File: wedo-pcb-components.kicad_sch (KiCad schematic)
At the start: 1 part, among them U1 TPS61032

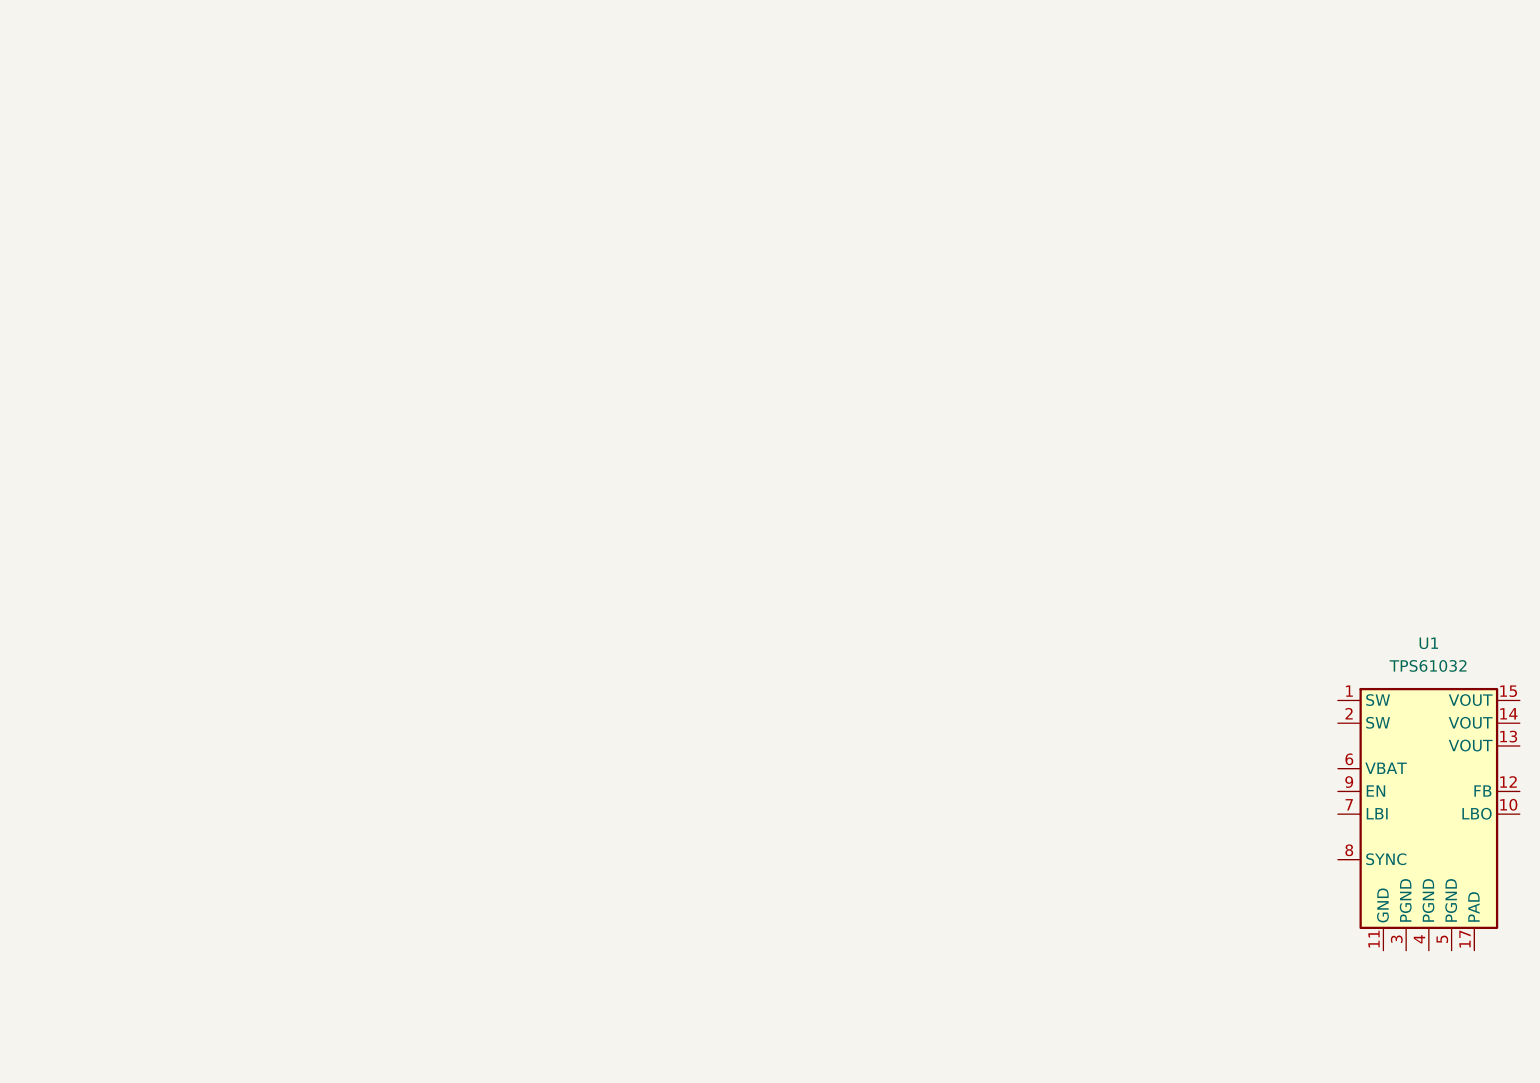
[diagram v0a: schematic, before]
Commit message: Add 6p6c connector footprint and adjust PCB geometry with mounting holes
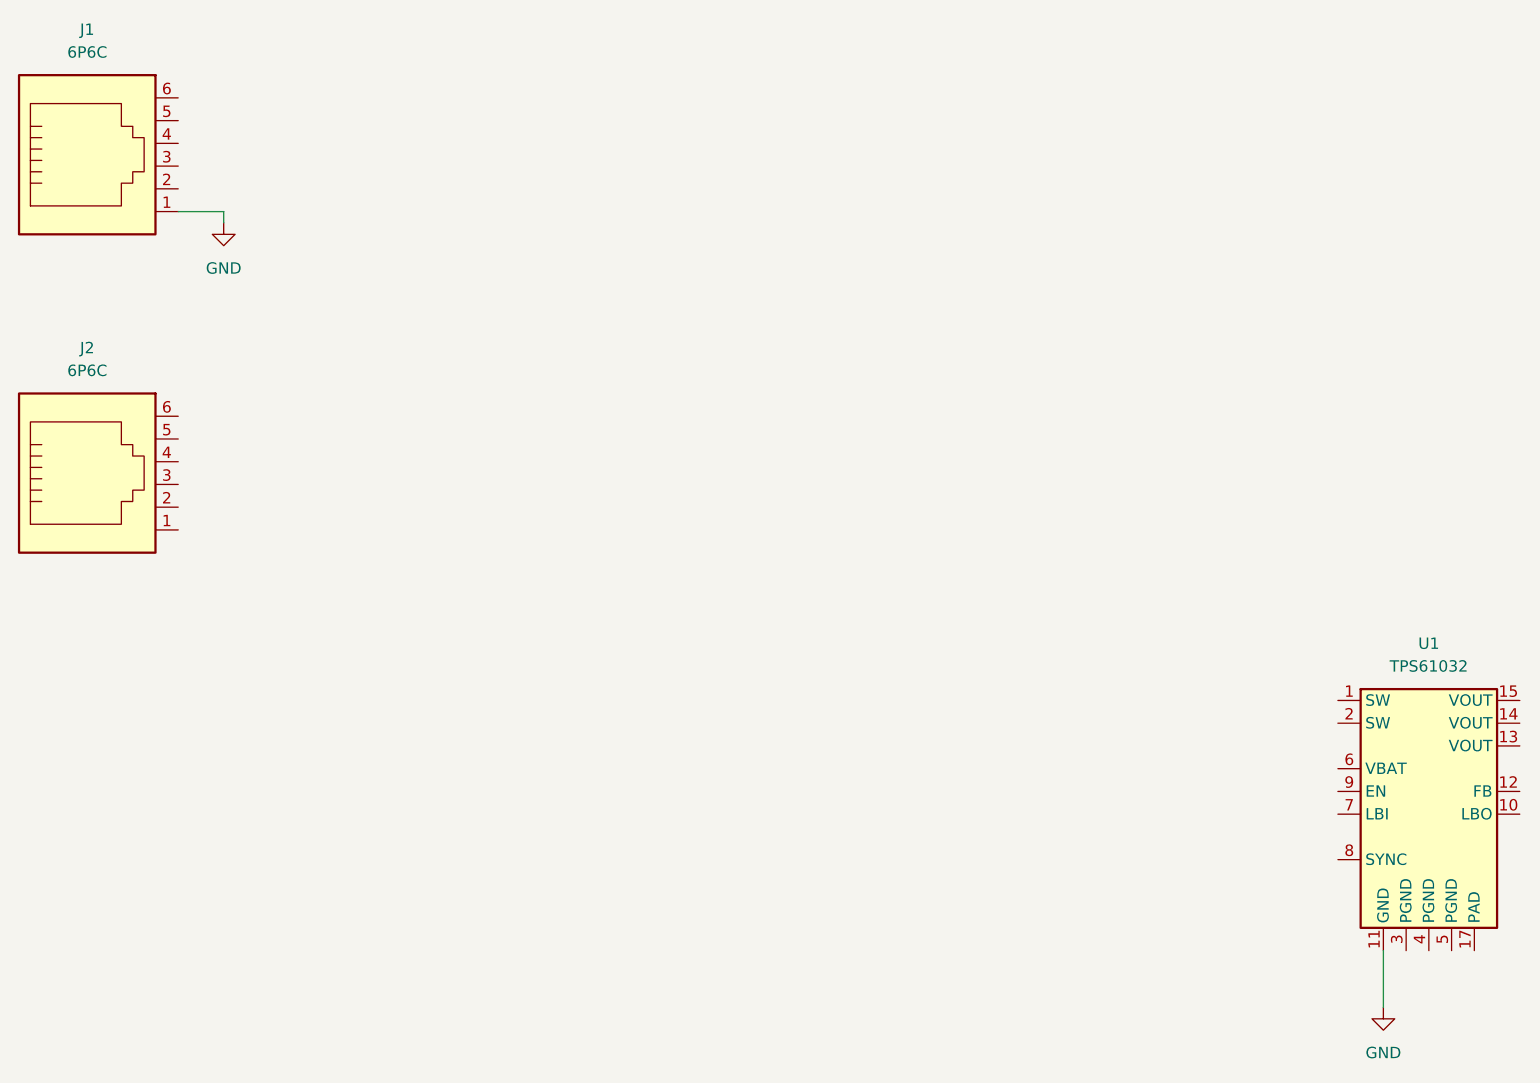
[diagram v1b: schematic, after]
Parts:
- added J1, J2: 6P6C, Connector_RJ_wedo:RJ12_wedo, symbol Connector:6P6C
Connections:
- net GND: now reaches U1.11 (GND)
- net GND: now also J1.1
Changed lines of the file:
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@@
 (kicad_sch (version 20230121) (generator eeschema)
   (paper "A4")
+  (wire (pts (xy 203.2 147.32) (xy 203.2 153.67))
+    (stroke (width 0) (type default))
+  )
+  (wire (pts (xy 73.66 64.77) (xy 73.66 66.04))
+    (stroke (width 0) (type default))
+  )
+  (wire (pts (xy 68.58 64.77) (xy 73.66 64.77))
+    (stroke (width 0) (type default))
+  )
   (symbol (lib_id "Regulator_Switching_Boost:TPS61032") (at 208.28 132.08 0) (unit 1)
     (in_bom yes) (on_board yes) (dnp no) (fields_autoplaced)
@@
         )
       )
+    )
+  )
+  (symbol (lib_id "power:GND") (at 203.2 153.67 0) (unit 1)
+    (in_bom yes) (on_board yes) (dnp no) (fields_autoplaced)
+    (property "Reference" "#PWR01" (at 203.2 160.02 0)
+      (effects (font (size 1.27 1.27)) hide)
+    )
+    (property "Value" "GND" (at 203.2 158.75 0)
+      (effects (font (size 1.27 1.27)))
+    )
+    (property "Footprint" "" (at 203.2 153.67 0)
+      (effects (font (size 1.27 1.27)) hide)
+    )
+    (property "Datasheet" "" (at 203.2 153.67 0)
+      (effects (font (size 1.27 1.27)) hide)
+    )
+    (pin "1")
+    (instances
+      (project "wedo-pcb-components"
+        (path "/3b24d53b-e226-431a-952a-6b8641a91fb3"
+          (reference "#PWR01") (unit 1)
+        )
+      )
+    )
+  )
+  (symbol (lib_id "power:GND") (at 73.66 66.04 0) (unit 1)
+    (in_bom yes) (on_board yes) (dnp no) (fields_autoplaced)
+    (property "Reference" "#PWR02" (at 73.66 72.39 0)
+      (effects (font (size 1.27 1.27)) hide)
+    )
+    (property "Value" "GND" (at 73.66 71.12 0)
+      (effects (font (size 1.27 1.27)))
+    )
+    (property "Footprint" "" (at 73.66 66.04 0)
+      (effects (font (size 1.27 1.27)) hide)
+    )
+    (property "Datasheet" "" (at 73.66 66.04 0)
+      (effects (font (size 1.27 1.27)) hide)
+    )
+    (pin "1")
+    (instances
+      (project "wedo-pcb-components"
+        (path "/3b24d53b-e226-431a-952a-6b8641a91fb3"
+          (reference "#PWR02") (unit 1)
+        )
+      )
+    )
+  )
+  (symbol (lib_id "Connector:6P6C") (at 58.42 95.25 0) (unit 1)
+    (in_bom yes) (on_board yes) (dnp no) (fields_autoplaced)
+    (property "Reference" "J2" (at 58.42 80.01 0)
+      (effects (font (size 1.27 1.27)))
+    )
+    (property "Value" "6P6C" (at 58.42 82.55 0)
+      (effects (font (size 1.27 1.27)))
+    )
+    (property "Footprint" "Connector_RJ_wedo:RJ12_wedo" (at 58.42 94.615 90)
+      (effects (font (size 1.27 1.27)) hide)
+    )
+    (property "Datasheet" "~" (at 58.42 94.615 90)
+      (effects (font (size 1.27 1.27)) hide)
+    )
+    (pin "3")
+    (pin "2")
+    (pin "4")
+    (pin "5")
+    (pin "6")
+    (pin "1")
+    (instances
+      (project "wedo-pcb-components"
+        (path "/3b24d53b-e226-431a-952a-6b8641a91fb3"
+          (reference "J2") (unit 1)
+        )
+      )
+    )
+  )
+  (symbol (lib_id "Connector:6P6C") (at 58.42 59.69 0) (unit 1)
+    (in_bom yes) (on_board yes) (dnp no) (fields_autoplaced)
+    (property "Reference" "J1" (at 58.42 44.45 0)
+      (effects (font (size 1.27 1.27)))
+    )
+    (property "Value" "6P6C" (at 58.42 46.99 0)
+      (effects (font (size 1.27 1.27)))
+    )
+    (property "Footprint" "Connector_RJ_wedo:RJ12_wedo" (at 58.42 59.055 90)
+      (effects (font (size 1.27 1.27)) hide)
+    )
+    (property "Datasheet" "~" (at 58.42 59.055 90)
+      (effects (font (size 1.27 1.27)) hide)
+    )
+    (pin "3")
+    (pin "2")
+    (pin "4")
+    (pin "5")
+    (pin "6")
+    (pin "1")
+    (instances
+      (project "wedo-pcb-components"
+        (path "/3b24d53b-e226-431a-952a-6b8641a91fb3"
+          (reference "J1") (unit 1)
+        )
+      )

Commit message: Adjusted PCB size, added battery blade connector, also added RGB LED and push button switch
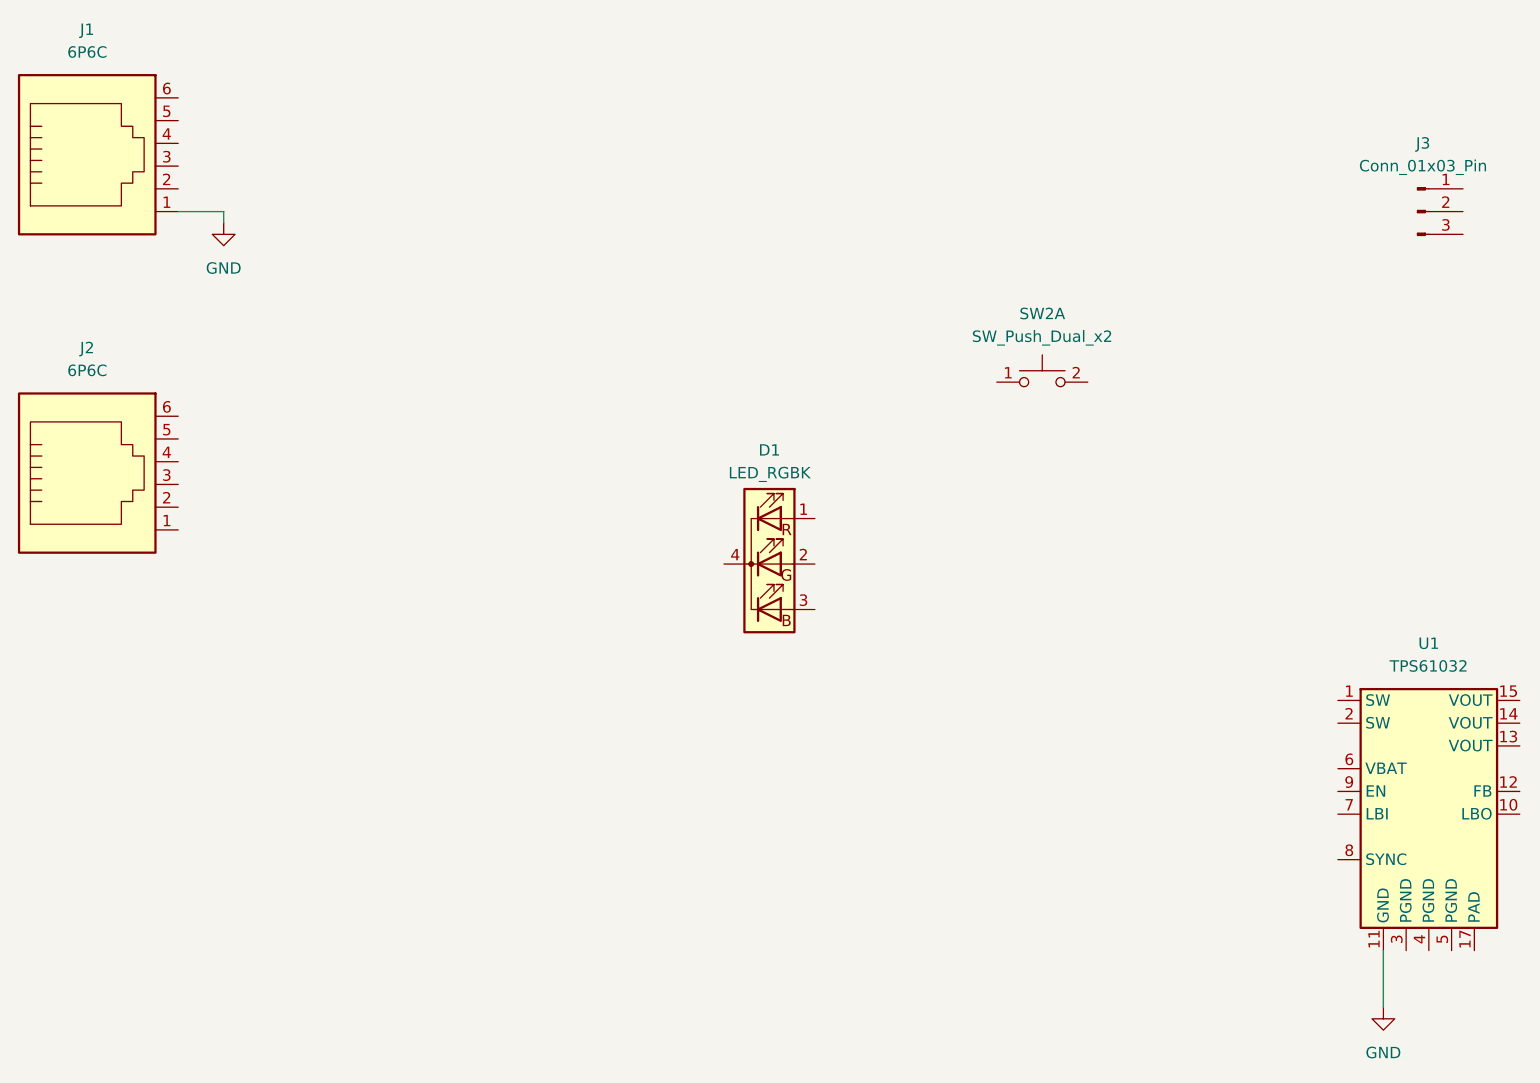
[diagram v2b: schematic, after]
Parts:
- added D1: LED_RGBK, LED_SMD:LED_RGB_Wuerth-PLCC4_3.2x2.8mm_150141M173100, symbol Device:LED_RGBK
- added J3: Conn_01x03_Pin, Connector_battery_blade:Male_RoundBlade_1x03_P2.0mm_Horizontal, symbol Connector:Conn_01x03_Pin
- added SW2: SW_Push_Dual_x2, Button_Switch_SMD:SW_Push_1P1T_XKB_TS-1187A, symbol Switch:SW_Push_Dual_x2
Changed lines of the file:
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@@
     (stroke (width 0) (type default))
+  )
+  (symbol (lib_id "Connector:Conn_01x03_Pin") (at 207.01 64.77 0) (unit 1)
+    (in_bom yes) (on_board yes) (dnp no) (fields_autoplaced)
+    (property "Reference" "J3" (at 207.645 57.15 0)
+      (effects (font (size 1.27 1.27)))
+    )
+    (property "Value" "Conn_01x03_Pin" (at 207.645 59.69 0)
+      (effects (font (size 1.27 1.27)))
+    )
+    (property "Footprint" "Connector_battery_blade:Male_RoundBlade_1x03_P2.0mm_Horizontal" (at 207.01 64.77 0)
+      (effects (font (size 1.27 1.27)) hide)
+    )
+    (property "Datasheet" "~" (at 207.01 64.77 0)
+      (effects (font (size 1.27 1.27)) hide)
+    )
+    (pin "3")
+    (pin "2")
+    (pin "1")
+    (instances
+      (project "wedo-pcb-components"
+        (path "/3b24d53b-e226-431a-952a-6b8641a91fb3"
+          (reference "J3") (unit 1)
+        )
+      )
+    )
   )
   (symbol (lib_id "Regulator_Switching_Boost:TPS61032") (at 208.28 132.08 0) (unit 1)
@@
         )
       )
+    )
+  )
+  (symbol (lib_id "Switch:SW_Push_Dual_x2") (at 165.1 83.82 0) (unit 1)
+    (in_bom yes) (on_board yes) (dnp no) (fields_autoplaced)
+    (property "Reference" "SW2" (at 165.1 76.2 0)
+      (effects (font (size 1.27 1.27)))
+    )
+    (property "Value" "SW_Push_Dual_x2" (at 165.1 78.74 0)
+      (effects (font (size 1.27 1.27)))
+    )
+    (property "Footprint" "Button_Switch_SMD:SW_Push_1P1T_XKB_TS-1187A" (at 165.1 78.74 0)
+      (effects (font (size 1.27 1.27)) hide)
+    )
+    (property "Datasheet" "~" (at 165.1 78.74 0)
+      (effects (font (size 1.27 1.27)) hide)
+    )
+    (pin "1")
+    (pin "2")
+    (pin "3")
+    (pin "4")
+    (instances
+      (project "wedo-pcb-components"
+        (path "/3b24d53b-e226-431a-952a-6b8641a91fb3"
+          (reference "SW2") (unit 1)
+        )
+      )
+    )
+  )
+  (symbol (lib_id "Device:LED_RGBK") (at 134.62 104.14 0) (unit 1)
+    (in_bom yes) (on_board yes) (dnp no) (fields_autoplaced)
+    (property "Reference" "D1" (at 134.62 91.44 0)
+      (effects (font (size 1.27 1.27)))
+    )
+    (property "Value" "LED_RGBK" (at 134.62 93.98 0)
+      (effects (font (size 1.27 1.27)))
+    )
+    (property "Footprint" "LED_SMD:LED_RGB_Wuerth-PLCC4_3.2x2.8mm_150141M173100" (at 134.62 105.41 0)
+      (effects (font (size 1.27 1.27)) hide)
+    )
+    (property "Datasheet" "~" (at 134.62 105.41 0)
+      (effects (font (size 1.27 1.27)) hide)
+    )
+    (pin "4")
+    (pin "1")
+    (pin "2")
+    (pin "3")
+    (instances
+      (project "wedo-pcb-components"
+        (path "/3b24d53b-e226-431a-952a-6b8641a91fb3"
+          (reference "D1") (unit 1)
+        )
+      )
